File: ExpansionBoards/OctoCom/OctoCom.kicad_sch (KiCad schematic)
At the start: 101 parts, among them J1 Conn_02x10_Odd_Even, J10 Conn_02x02_Odd_Even, J11 Conn_02x02_Odd_Even, J12 Conn_02x02_Odd_Even, J13 Conn_02x02_Odd_Even, J14 DPD-09-11-B3, J15 Conn_02x02_Odd_Even, J16 Conn_02x02_Odd_Even, J17 Conn_02x02_Odd_Even, J18 Conn_02x02_Odd_Even, J19 Conn_02x02_Odd_Even, J2 Conn_02x20_Odd_Even, J20 Conn_02x02_Odd_Even, J21 DPD-09-11-B3, J22 Conn_02x02_Odd_Even, J23 Conn_02x02_Odd_Even, J24 Conn_02x02_Odd_Even, J25 Conn_02x02_Odd_Even, J26 Conn_02x02_Odd_Even, J27 Conn_02x02_Odd_Even, J28 DPD-09-11-B3, J29 Conn_02x02_Odd_Even, J30 Conn_02x02_Odd_Even, J31 Conn_02x02_Odd_Even, J32 Conn_02x04_Odd_Even, J33 4-171826-4, J34 Conn_02x03_Odd_Even, J4 DPD-09-11-B3, J5 Conn_02x02_Odd_Even, J6 Conn_02x02_Odd_Even, J7 Conn_02x02_Odd_Even, J8 Conn_02x02_Odd_Even, J9 Conn_02x02_Odd_Even, U1 ST16C554D, U10 SP3243EEY, U11 SP3243EEY, U12 74LS74, U14 SP3243EEY, U16 74LS00, U2 74LS139, U3 74HCT138, U4 SP3243EEY, U5 SP3243EEY, U6 SP3243EEY, U7 SP3243EEY, U8 SP3243EEY, U9 ST16C554D, X1 1.8432M, X1-ALT 1.8432M

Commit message: rework octocom logic to use 22V10 for speed
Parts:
- removed C43: 33n, Capacitor_SMD:C_0805_2012Metric_Pad1.18x1.45mm_HandSolder, symbol Device:C_Small
- removed D1: 4148, Diode_THT:D_DO-35_SOD27_P7.62mm_Horizontal, symbol Diode:1N4148
- removed J32: Conn_02x04_Odd_Even, Connector_PinHeader_2.54mm:PinHeader_2x04_P2.54mm_Vertical, symbol Connector_Generic:Conn_02x04_Odd_Even
- removed J34: Conn_02x03_Odd_Even, Connector_PinHeader_2.54mm:PinHeader_2x03_P2.54mm_Vertical, symbol Connector_Generic:Conn_02x03_Odd_Even
- removed U12: 74LS74, Package_DIP:DIP-14_W7.62mm, symbol 74xx:74LS74
- removed U16: 74LS00, Package_DIP:DIP-14_W7.62mm, symbol 74xx:74LS00
- removed U2: 74LS139, Package_DIP:DIP-16_W7.62mm, symbol 74xx:74LS139
- added H1: M3, MountingHole:MountingHole_3.2mm_M3_Pad_Via, symbol Mechanical:MountingHole_Pad
- added J32: Conn_01x02, Connector_PinHeader_2.54mm:PinHeader_1x02_P2.54mm_Vertical, symbol Connector_Generic:Conn_01x02
- added J34, J35, J36: Conn_01x03, Connector_PinHeader_2.54mm:PinHeader_1x03_P2.54mm_Vertical, symbol Connector_Generic:Conn_01x03
- added J37: Conn_02x04_Odd_Even, Connector_PinHeader_2.54mm:PinHeader_2x04_P2.54mm_Vertical, symbol Connector_Generic:Conn_02x04_Odd_Even
- added U13: SN74AHCT125, Package_SO:SO-14_3.9x8.65mm_P1.27mm, symbol 74xx:74AHCT125
- added U2: ATF22V10, Package_DIP:DIP-24_W7.62mm, symbol Logic_Programmable:PAL20RS10
- U3: value 74HCT138 -> 74F138; Mouser (none) -> 595-SN74F138N
- renumbered X1-ALT to ALT-X1
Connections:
- net CPU-A20: now also U2.6 (I4)
- net CPU-A21: now also U2.7 (I5)
- net CPU-A22: now also U2.8 (I6)
- net CPU-A23: now also U2.20 (O3)
- net CPU-A31: now also U2.5 (I3)
- net CPU-CLK: now also U2.1 (CLK)
- net CPU-R/~{W}: now also U2.3 (I1)
- net GND: now also H1.1, J32.2 (Pin_2), J34.3 (Pin_3), J35.3 (Pin_3), J36.3 (Pin_3), U13.12, U13.2, U13.7 (GND), U13.9, U2.12 (GND)
- net IO-RESET: now also U13.6
- net VCC: now also J34.1 (Pin_1), J35.1 (Pin_1), J36.1 (Pin_1), U13.13, U13.14 (VCC), U13.5, U2.24 (VCC)
- net ~{CPU-AS}: now also U2.2 (I0)
- net ~{CPU-DSACK0}: now also U13.3
- net ~{CPU-DS}: now also U2.4 (I2)
- net ~{CPU-RESET}: now also U13.4
- net ~{IO-CE}: now also J37.1 (Pin_1), U13.10, U2.21 (O2)
- net ~{IORD}: now also U2.23 (O0)
- net ~{IOWR}: now also U2.22 (O1)
- new net: J37.2 (Pin_2), J37.4 (Pin_4), J37.6 (Pin_6), J37.8 (Pin_8), U13.1
- new net IOSEL0: J34.2 (Pin_2), U2.9 (I7)
- new net IOSEL1: J35.2 (Pin_2), U2.10 (I8)
- new net IOSEL2: J36.2 (Pin_2), U2.11 (I9)
- new net ~{1WS}: J37.7 (Pin_7), U2.14 (O9)
- new net ~{2WS}: J37.5 (Pin_5), U2.15 (O8)
- new net ~{3WS}: J37.3 (Pin_3), U2.16 (O7)
- new net ~{CPU-CIIN}: J32.1 (Pin_1), U13.8
- no-connect marks 0 -> 3
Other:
- moved on the sheet: C41, C42, C44, C45, C46, H2, H3, H4, J33, U3

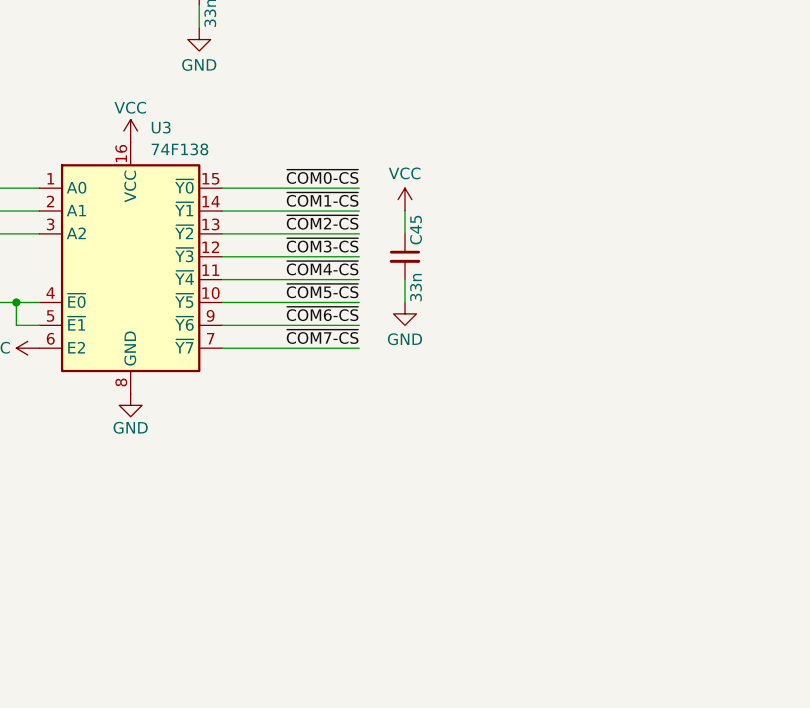
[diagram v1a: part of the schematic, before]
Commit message: Add device selection LEDs
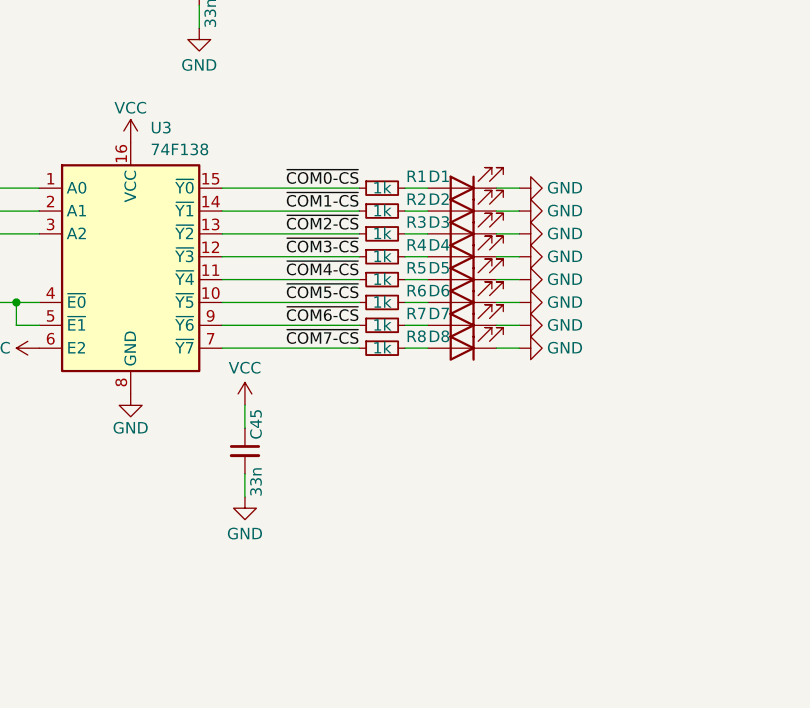
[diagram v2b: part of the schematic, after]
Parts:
- added D1, D2, D3, D4, D5, D6, D7, D8: LED, LED_SMD:LED_1210_3225Metric_Pad1.42x2.65mm_HandSolder, symbol Device:LED
- added R1, R2, R3, R4, R5, R6, R7, R8: 1k, Resistor_SMD:R_0805_2012Metric_Pad1.20x1.40mm_HandSolder, symbol Device:R_Small
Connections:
- net GND: now also D1.1 (K), D2.1 (K), D3.1 (K), D4.1 (K), D5.1 (K), D6.1 (K), D7.1 (K), D8.1 (K)
- net ~{COM0-CS}: now also R1.1
- net ~{COM1-CS}: now also R2.1
- net ~{COM2-CS}: now also R3.1
- net ~{COM3-CS}: now also R4.1
- net ~{COM4-CS}: now also R5.1
- net ~{COM5-CS}: now also R6.1
- net ~{COM6-CS}: now also R7.1
- net ~{COM7-CS}: now also R8.1
- new net: D4.2 (A), R4.2
- new net: D5.2 (A), R5.2
- new net: D1.2 (A), R1.2
- new net: D7.2 (A), R7.2
- new net: D8.2 (A), R8.2
- new net: D6.2 (A), R6.2
- new net: D2.2 (A), R2.2
- new net: D3.2 (A), R3.2
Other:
- moved on the sheet: C45

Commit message: Move from DE9 to RJ45 for serial ports
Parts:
- removed J14, J21, J28, J4: DPD-09-11-B3, OctoCom:DPD-09-11-B3, symbol OctoCom:DPD-09-11-B3
- added C43, C49, C50: 33n, Capacitor_SMD:C_0805_2012Metric_Pad1.18x1.45mm_HandSolder, symbol Device:C_Small
- added J3, J4: 8P8C_LED_Shielded_x4, OctoCom:CRJ047-L3-TH, symbol OctoCom:8P8C_LED_Shielded_x2
- added R10, R11, R12, R13, R14, R15, R16, R17, R18, R19, R20, R21, R22, R23, R24, R9: 180, Resistor_SMD:R_1206_3216Metric_Pad1.30x1.75mm_HandSolder, symbol Device:R_Small
- added U12, U15, U16: 74HC240, Package_SO:TSSOP-20_4.4x6.5mm_P0.65mm, symbol 74xx:74LS240
- D1, D2, D3, D4, D5, D6, D7, D8: footprint LED_SMD:LED_1210_3225Metric_Pad1.42x2.65mm_HandSolder -> LED_SMD:LED_1206_3216Metric_Pad1.42x1.75mm_HandSolder
- R1, R2, R3, R4, R5, R6, R7, R8: value 1k -> 180; footprint Resistor_SMD:R_0805_2012Metric_Pad1.20x1.40mm_HandSolder -> Resistor_SMD:R_1206_3216Metric_Pad1.30x1.75mm_HandSolder; Mouser (none) -> 660-RK73B2BTTE181J
- U13: value SN74AHCT125 -> 74AHCT125
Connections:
- net COM0-P2: now also J3.D6
- net COM0-P3: now also J3.D3
- net COM0-P4: now also J3.D2
- net COM0-P6: now also J3.D7
- net COM0-P7: now also J3.D1
- net COM0-P8: now also J3.D8
- net COM0-RX: now also U12.4 (I1a)
- net COM0-TX: now also U12.2 (I0a)
- net COM1-P2: now also J3.C6
- net COM1-P3: now also J3.C3
- net COM1-P4: now also J3.C2
- net COM1-P6: now also J3.C7
- net COM1-P7: now also J3.C1
- net COM1-P8: now also J3.C8
- net COM1-RX: now also U12.8 (I3a)
- net COM1-TX: now also U12.6 (I2a)
- net COM2-P2: now also J4.A6
- net COM2-P3: now also J4.A3
- net COM2-P4: now also J4.A2
- net COM2-P6: now also J4.A7
- net COM2-P7: now also J4.A1
- net COM2-P8: now also J4.A8
- net COM2-RX: now also U15.4 (I1a)
- net COM2-TX: now also U15.2 (I0a)
- net COM3-P2: now also J4.B6
- net COM3-P3: now also J4.B3
- net COM3-P4: now also J4.B2
- net COM3-P6: now also J4.B7
- net COM3-P7: now also J4.B1
- net COM3-P8: now also J4.B8
- net COM3-RX: now also U15.8 (I3a)
- net COM3-TX: now also U15.6 (I2a)
- net COM4-P2: now also J3.B6
- net COM4-P3: now also J3.B3
- net COM4-P4: now also J3.B2
- net COM4-P6: now also J3.B7
- net COM4-P7: now also J3.B1
- net COM4-P8: now also J3.B8
- net COM4-RX: now also U12.13 (I1b)
- net COM4-TX: now also U12.11 (I0b)
- net COM5-P2: now also J3.A6
- net COM5-P3: now also J3.A3
- net COM5-P4: now also J3.A2
- net COM5-P6: now also J3.A7
- net COM5-P7: now also J3.A1
- net COM5-P8: now also J3.A8
- net COM5-RX: now also U12.17 (I3b)
- net COM5-TX: now also U12.15 (I2b)
- net COM6-P2: now also J4.C6
- net COM6-P3: now also J4.C3
- net COM6-P4: now also J4.C2
- net COM6-P6: now also J4.C7
- net COM6-P7: now also J4.C1
- net COM6-P8: now also J4.C8
- net COM6-RX: now also U15.13 (I1b)
- net COM6-TX: now also U15.11 (I0b)
- net COM7-P2: now also J4.D6
- net COM7-P3: now also J4.D3
- net COM7-P4: now also J4.D2
- net COM7-P6: now also J4.D7
- net COM7-P7: now also J4.D1
- net COM7-P8: now also J4.D8
- net COM7-RX: now also U15.17 (I3b)
- net COM7-TX: now also U15.15 (I2b)
- net GND: now also C43.2, C49.2, C50.2, J3.A11, J3.A4, J3.A5, J3.A9, J3.B11, J3.B4, J3.B5, J3.B9, J3.C11, J3.C4, J3.C5, J3.C9, J3.D11, J3.D4, J3.D5, J3.D9, J3.SH, J3.SH, J3.SH, J3.SH, J4.A11, J4.A4, J4.A5, J4.A9, J4.B11, J4.B4, J4.B5, J4.B9, J4.C11, J4.C4, J4.C5, J4.C9, J4.D11, J4.D4, J4.D5, J4.D9, J4.SH, J4.SH, J4.SH, J4.SH, U12.1 (OEa), U12.10 (GND), U12.19 (OEb), U15.1 (OEa), U15.10 (GND), U15.19 (OEb), U16.1 (OEa), U16.10 (GND), U16.19 (OEb)
- net VCC: now also C43.1, C49.1, C50.1, U12.20 (VCC), U15.20 (VCC), U16.20 (VCC)
- net ~{COM0-CS}: now also U16.2 (I0a); no longer R1.1
- net ~{COM1-CS}: now also U16.4 (I1a); no longer R2.1
- net ~{COM2-CS}: now also U9.7 (~{CSA}), U16.6 (I2a); no longer R3.1, U1.38 (~{CSC})
- net ~{COM3-CS}: now also U9.11 (~{CSB}), U16.8 (I3a); no longer R4.1, U1.42 (~{CSD})
- net ~{COM4-CS}: now also U1.38 (~{CSC}), U16.11 (I0b); no longer R5.1, U9.7 (~{CSA})
- net ~{COM5-CS}: now also U1.42 (~{CSD}), U16.13 (I1b); no longer R6.1, U9.11 (~{CSB})
- net ~{COM6-CS}: now also U16.15 (I2b); no longer R7.1
- net ~{COM7-CS}: now also U16.17 (I3b); no longer R8.1
- net COM1-RX-lED: now reaches R4.2
- net COM1-RX-lED: now also J3.C12; no longer D4.2 (A)
- net COM2-TX-LED: now reaches R5.2
- net COM2-TX-LED: now also J4.A10; no longer D5.2 (A)
- net COM0-CS-LED: now reaches D1.2 (A)
- net COM0-CS-LED: now also R17.2; no longer R1.2
- net COM3-TX-LED: now reaches R7.2
- net COM3-TX-LED: now also J4.B10; no longer D7.2 (A)
- net COM3-RX-lED: now reaches R8.2
- net COM3-RX-lED: now also J4.B12; no longer D8.2 (A)
- net COM2-RX-lED: now reaches R6.2
- net COM2-RX-lED: now also J4.A12; no longer D6.2 (A)
- net COM0-RX-lED: now reaches R2.2
- net COM0-RX-lED: now also J3.D12; no longer D2.2 (A)
- net COM1-TX-LED: now reaches R3.2
- net COM1-TX-LED: now also J3.C10; no longer D3.2 (A)
- new net COM0-CS-LED-R: R17.1, U16.18 (O0a)
- new net COM0-RX-LED-R: R2.1, U12.16 (O1a)
- new net COM0-TX-LED: J3.D10, R1.2
- new net COM0-TX-LED-R: R1.1, U12.18 (O0a)
- new net COM1-CS-LED: D2.2 (A), R18.2
- new net COM1-CS-LED-R: R18.1, U16.16 (O1a)
- new net COM1-RX-LED-R: R4.1, U12.12 (O3a)
- new net COM1-TX-LED-R: R3.1, U12.14 (O2a)
- new net COM2-CS-LED: D3.2 (A), R19.2
- new net COM2-CS-LED-R: R19.1, U16.14 (O2a)
- new net COM2-RX-LED-R: R6.1, U15.16 (O1a)
- new net COM2-TX-LED-R: R5.1, U15.18 (O0a)
- new net COM3-CS-LED: D4.2 (A), R20.2
- new net COM3-CS-LED-R: R20.1, U16.12 (O3a)
- new net COM3-RX-LED-R: R8.1, U15.12 (O3a)
- new net COM3-TX-LED-R: R7.1, U15.14 (O2a)
- new net COM4-CS-LED: D5.2 (A), R21.2
- new net COM4-CS-LED-R: R21.1, U16.9 (O0b)
- new net COM4-RX-LED-R: R10.1, U12.7 (O1b)
- new net COM4-RX-lED: J3.B12, R10.2
- new net COM4-TX-LED: J3.B10, R9.2
- new net COM4-TX-LED-R: R9.1, U12.9 (O0b)
- new net COM5-CS-LED: D6.2 (A), R22.2
- new net COM5-CS-LED-R: R22.1, U16.7 (O1b)
- new net COM5-RX-LED-R: R12.1, U12.3 (O3b)
- new net COM5-RX-lED: J3.A12, R12.2
- new net COM5-TX-LED: J3.A10, R11.2
- new net COM5-TX-LED-R: R11.1, U12.5 (O2b)
- new net COM6-CS-LED: D7.2 (A), R23.2
- new net COM6-CS-LED-R: R23.1, U16.5 (O2b)
- new net COM6-RX-LED-R: R14.1, U15.7 (O1b)
- new net COM6-RX-lED: J4.C12, R14.2
- new net COM6-TX-LED: J4.C10, R13.2
- new net COM6-TX-LED-R: R13.1, U15.9 (O0b)
- new net COM7-CS-LED: D8.2 (A), R24.2
- new net COM7-CS-LED-R: R24.1, U16.3 (O3b)
- new net COM7-RX-LED-R: R16.1, U15.3 (O3b)
- new net COM7-RX-lED: J4.D12, R16.2
- new net COM7-TX-LED: J4.D10, R15.2
- new net COM7-TX-LED-R: R15.1, U15.5 (O2b)
